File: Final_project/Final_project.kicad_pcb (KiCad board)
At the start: 2 copper layers, 66 x 37 mm, 56 parts, among them J1 USB4105-GF-A, J2 Conn_01x04, J4 LEFT, J5 RIGHT, U1 RP2040, U2 MCP1702T-3302E_CB, U3 W25Q128JV, U4 ESP32-WROOM-32, U5 LM393D, Y1 12MHz

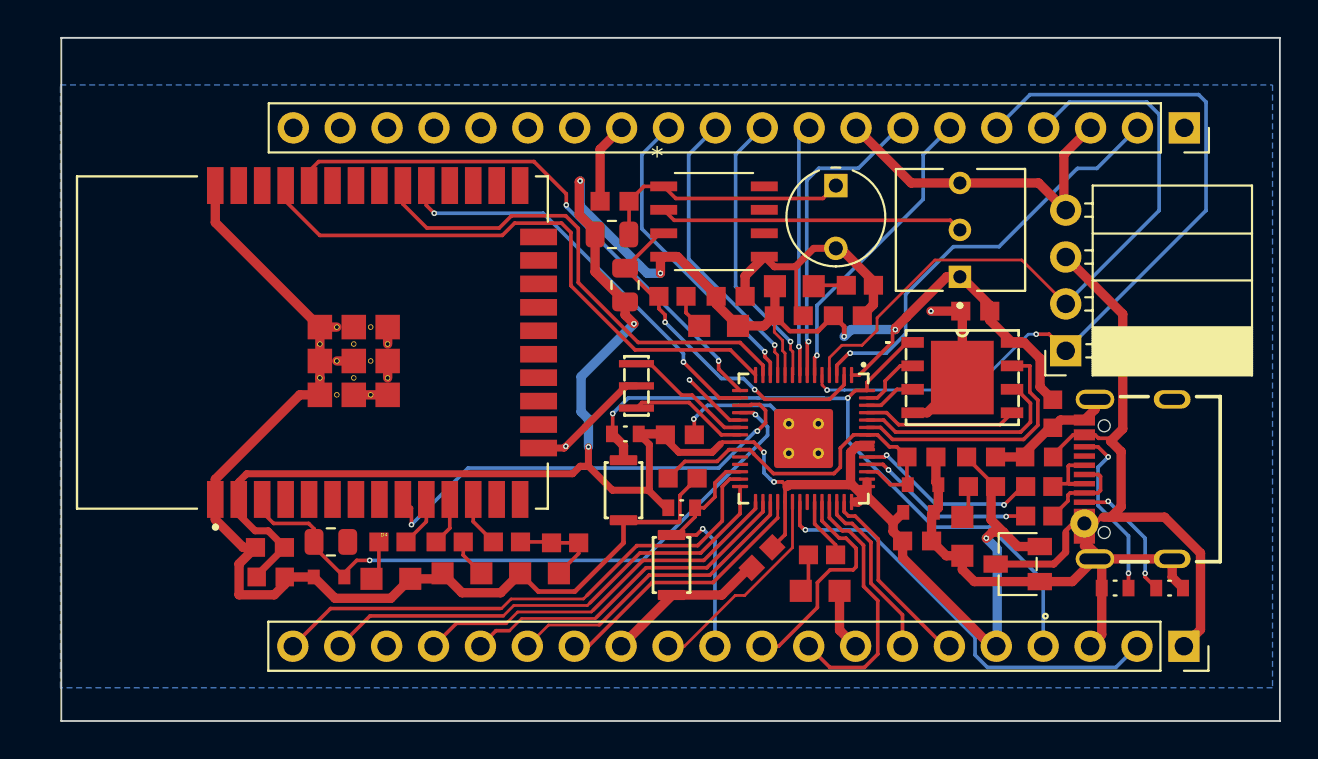
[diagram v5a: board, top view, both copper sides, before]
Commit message: Add 3d, fixing vias and layout issues
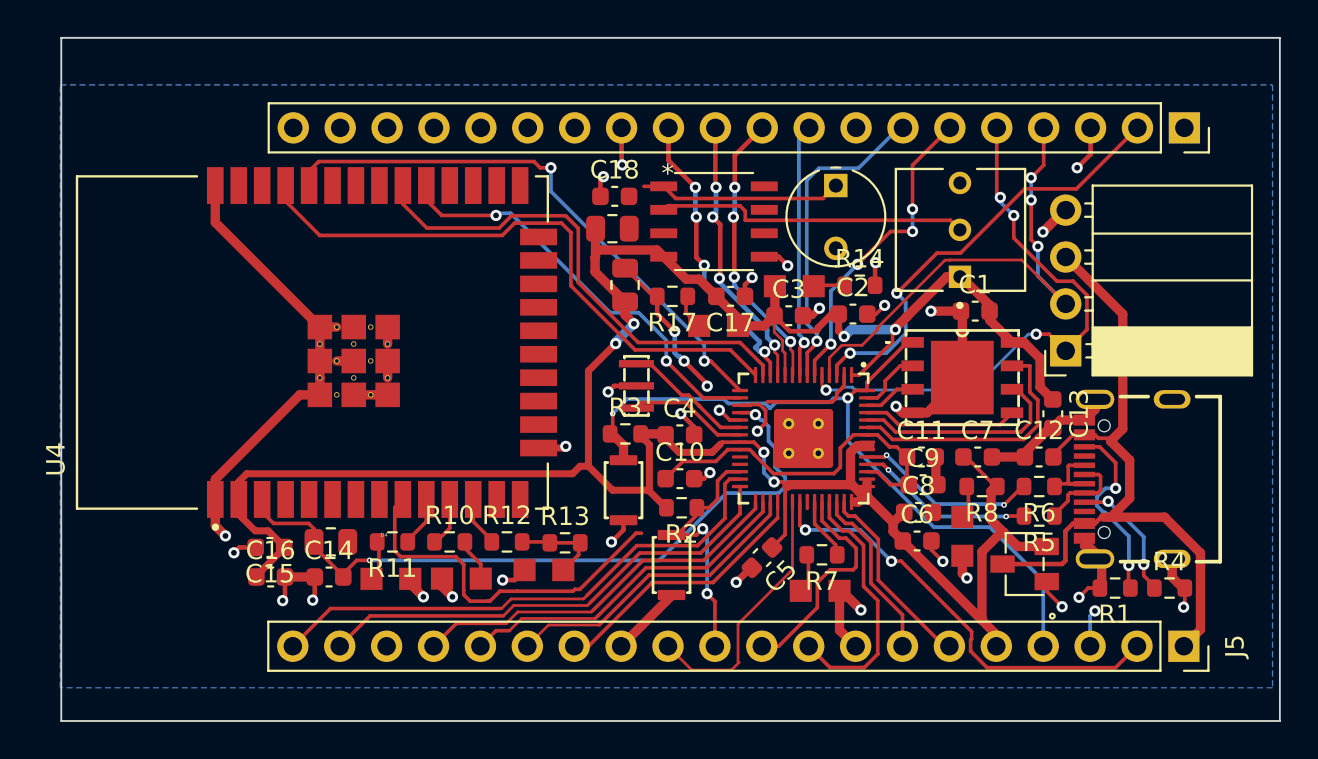
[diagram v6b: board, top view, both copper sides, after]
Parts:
- C1, C10, C11, C15, C17, C18, C2, C3, C4, C5, C6, C7: footprint Final_project:CL10B104JB8NNNC -> Capacitor_SMD:C_0603_1608Metric
- C12, C13, C16: footprint Final_project:GRM188R61E106KA73D -> Capacitor_SMD:C_0603_1608Metric
- C14, C8, C9: footprint Final_project:CL10B105KA8NNNC -> Capacitor_SMD:C_0603_1608Metric
- R1, R2, R3, R4: footprint Final_project:RES_ERJ3EKF5101V -> Resistor_SMD:R_0603_1608Metric
- R10, R11, R12, R13, R14, R17, R5, R6, R7, R8: footprint Final_project:RC0603FR-071KL -> Resistor_SMD:R_0603_1608Metric
- R9: value 10K R -> 10K
- moved U2 0.37 mm to (142.8, 87.2)
- moved R15 0.31 mm to (120.4, 69.0)
- moved D5 0.29 mm to (116.7, 87.5)
- moved C2 0.29 mm to (133.5, 73.7)
- moved D3 0.29 mm to (112.3, 88.0)
- moved C18 0.27 mm to (120.6, 67.3)
- moved C7 0.18 mm to (140.2, 81.4)
- moved C10 0.15 mm to (124.1, 82.6)
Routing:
- net GND: track 177.9 -> 104.2 mm, vias 4 -> 32
- net /GPIO3: track 44.3 -> 30.7 mm, vias 2 -> 4
- net /GPIO2: track 36.8 -> 27.6 mm, vias 0 -> 3
- net +3V3: track 150.0 -> 141.2 mm, vias 9 -> 6
- net /GPIO0: track 19.2 -> 14.0 mm, vias 2 -> 3
- net /GPIO22: track 11.4 -> 14.5 mm
- net /GPIO15: track 35.7 -> 38.7 mm
- net /Light_Sensing/AO: track 13.9 -> 11.0 mm
- net /GPIO14: track 25.2 -> 22.9 mm, vias 2 -> 1
- net /GPIO8: track 16.0 -> 15.0 mm, vias 1 -> 4
- net /GPIO9: track 16.9 -> 16.0 mm, vias 1 -> 4
- net Net-(J1-PadB5): track 9.53 -> 10.3 mm
- net /GPIO1: track 23.5 -> 24.2 mm, vias 1 -> 2
- net /GPIO4: track 16.4 -> 17.1 mm, vias 1 -> 4
- net /GPIO12: track 30.2 -> 30.7 mm
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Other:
- board text added: "Spotify Reader with Light/Dark Sensing Lauren Xiong and Melissa Kazazic Eclectronics FA 2022"

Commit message: fixed several problems
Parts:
- moved R16 1.11 mm to (120.4, 71.2), turned to 180 degrees
- moved C10 0.28 mm to (123.8, 82.5)
- moved R3 0.15 mm to (121.0, 80.2)
- moved R14 0.11 mm to (133.8, 72.0)
- turned R15 to 180 degrees
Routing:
- net /GPIO0: track 14.0 -> 27.4 mm, vias 3 -> 4
- net /GPIO14: track 22.9 -> 32.9 mm, vias 1 -> 2
- net GND: track 104.2 -> 111.1 mm, vias 32 -> 31
- net /Light_Sensing/AO: track 11.0 -> 14.5 mm
- net /GPIO15: track 38.7 -> 35.8 mm
- net +3V3: track 141.2 -> 142.8 mm
- net /GPIO13: track 23.0 -> 23.9 mm
- net /GPIO12: track 30.7 -> 31.4 mm
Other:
- board size 66 x 37 mm -> 66 x 34.6 mm

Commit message: rewired some GND pins
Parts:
- moved C9 0.22 mm to (137.1, 82.9)
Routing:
- net GND: track 111.1 -> 109.9 mm, vias 31 -> 33
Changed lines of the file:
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@@
   )
   (footprint "Capacitor_SMD:C_0603_1608Metric" (layer "F.Cu")
-    (at 137.2722 82.9)
+    (at 137.05 82.9)
     (descr "Capacitor SMD 0603 (1608 Metric), square (rectangular) end terminal, IPC_7351 nominal, (Body size source: IPC-SM-782 page 76, https://www.pcb-3d.com/wordpress/wp-content/uploads/ipc-sm-782a_amendment_1_and_2.pdf), generated with kicad-footprint-generator")
     (tags "capacitor")
@@
   (segment (start 139.4 73.584) (end 139.316 73.5) (width 0.508) (layer "F.Cu") (net 1))
   (segment (start 98.94 66.7) (end 98.94 68.7) (width 0.508) (layer "F.Cu") (net 1))
+  (segment (start 137.026125 85.176675) (end 137.8028 84.4) (width 0.2) (layer "F.Cu") (net 1))
   (segment (start 144.8054 89.5096) (end 143.9686 88.6728) (width 0.2) (layer "F.Cu") (net 1))
-  (segment (start 137.968 82.768) (end 138.1 82.9) (width 0.508) (layer "F.Cu") (net 1))
   (segment (start 137.495 79.005) (end 136.7076 79.005) (width 0.508) (layer "F.Cu") (net 1))
   (segment (start 132.317538 72.85) (end 133.775 72.85) (width 0.2) (layer "F.Cu") (net 1))
@@
   (segment (start 116.45 80.915) (end 117.831 80.915) (width 0.381) (layer "F.Cu") (net 1))
   (segment (start 126.800706 79.4) (end 127.3625 79.4) (width 0.2) (layer "F.Cu") (net 1))
+  (segment (start 137.959 81.4) (end 137.959 81.559) (width 0.2) (layer "F.Cu") (net 1))
   (segment (start 150.765 86.92) (end 150.765 87.915) (width 0.508) (layer "F.Cu") (net 1))
   (segment (start 98.94 68.7) (end 104.605 74.365) (width 0.508) (layer "F.Cu") (net 1))
@@
   (segment (start 135.280132 73.102175) (end 134.722307 73.66) (width 0.2) (layer "F.Cu") (net 1))
   (segment (start 144.949 68.03) (end 145 68.03) (width 0.508) (layer "F.Cu") (net 1))
+  (segment (start 137.959 81.559) (end 138.65 82.25) (width 0.2) (layer "F.Cu") (net 1))
   (segment (start 124.875 79.7741) (end 124.1552 79.0543) (width 0.25) (layer "F.Cu") (net 1))
   (segment (start 146.85 88.5) (end 146.2214 88.5) (width 0.2) (layer "F.Cu") (net 1))
@@
   (segment (start 128.67415 70.555) (end 129.455 70.555) (width 0.25) (layer "F.Cu") (net 1))
   (segment (start 143.9686 88.6728) (end 143.9686 88.148201) (width 0.2) (layer "F.Cu") (net 1))
+  (segment (start 137.825 82.9) (end 138 82.9) (width 0.381) (layer "F.Cu") (net 1))
   (segment (start 146.585 78.825) (end 146.01 79.4) (width 0.508) (layer "F.Cu") (net 1))
   (segment (start 108.275 77.1175) (end 108.275 76.2) (width 0.508) (layer "F.Cu") (net 1))
@@
   (segment (start 111.218 87.9856) (end 111.218 88.4088) (width 0.508) (layer "F.Cu") (net 1))
   (segment (start 124.875 80.2) (end 124.875 79.7741) (width 0.25) (layer "F.Cu") (net 1))
-  (segment (start 137.8028 84.4) (end 137.8028 85.8722) (width 0.381) (layer "F.Cu") (net 1))
   (segment (start 131.417538 73.75) (end 132.317538 72.85) (width 0.2) (layer "F.Cu") (net 1))
   (segment (start 123.65 88.875) (end 123.65 88.92) (width 0.508) (layer "F.Cu") (net 1))
@@
   (segment (start 98.94 85.1224) (end 99.4918 85.6742) (width 0.508) (layer "F.Cu") (net 1))
   (segment (start 127.626 72.7) (end 127.626 72.0688) (width 0.25) (layer "F.Cu") (net 1))
-  (segment (start 137.968 81.4) (end 137.968 82.768) (width 0.508) (layer "F.Cu") (net 1))
   (segment (start 146.95 88.5) (end 146.95 87.285) (width 0.508) (layer "F.Cu") (net 1))
   (segment (start 120.5446 77.55) (end 120.2182 77.8764) (width 0.25) (layer "F.Cu") (net 1))
@@
   (segment (start 137.734 84.5216) (end 137.8556 84.4) (width 0.508) (layer "F.Cu") (net 1))
   (segment (start 106.44 76.2) (end 105.5225 76.2) (width 0.508) (layer "F.Cu") (net 1))
+  (segment (start 136.982273 85.176675) (end 137.026125 85.176675) (width 0.2) (layer "F.Cu") (net 1))
   (segment (start 136.159611 79.005) (end 135.810034 78.655423) (width 0.508) (layer "F.Cu") (net 1))
   (segment (start 133.775 72.85) (end 134.625 72) (width 0.2) (layer "F.Cu") (net 1))
@@
   (segment (start 121.75 77.55) (end 120.5446 77.55) (width 0.25) (layer "F.Cu") (net 1))
   (segment (start 121.05 84.825) (end 121.05 85.3504) (width 0.254) (layer "F.Cu") (net 1))
-  (segment (start 138.0472 82.9) (end 138.0472 84.1556) (width 0.381) (layer "F.Cu") (net 1))
   (segment (start 146.01 79.4) (end 144.718 79.4) (width 0.508) (layer "F.Cu") (net 1))
   (segment (start 132.75 88.65) (end 132.8714 88.65) (width 0.508) (layer "F.Cu") (net 1))
@@
   (segment (start 137.8028 85.8722) (end 137.725 85.95) (width 0.381) (layer "F.Cu") (net 1))
   (segment (start 144.9 67.93) (end 145 68.03) (width 0.508) (layer "F.Cu") (net 1))
+  (segment (start 138 82.9) (end 138.65 82.25) (width 0.1524) (layer "F.Cu") (net 1))
   (segment (start 134.585 71.886976) (end 134.585 72.1) (width 0.508) (layer "F.Cu") (net 1))
+  (segment (start 136.982273 85.207273) (end 136.982273 85.176675) (width 0.2) (layer "F.Cu") (net 1))
   (segment (start 98.94 83.7) (end 98.94 85.1224) (width 0.508) (layer "F.Cu") (net 1))
   (segment (start 132.75 88.65) (end 132.75 90.78) (width 0.508) (layer "F.Cu") (net 1))
+  (segment (start 137.825 84.3778) (end 137.8028 84.4) (width 0.381) (layer "F.Cu") (net 1))
   (segment (start 125.714852 82.264852) (end 125.529704 82.45) (width 0.25) (layer "F.Cu") (net 1))
-  (segment (start 138.0472 84.1556) (end 137.8028 84.4) (width 0.381) (layer "F.Cu") (net 1))
   (segment (start 143.764 69.215) (end 144.949 68.03) (width 0.508) (layer "F.Cu") (net 1))
   (segment (start 119.7988 67.2846) (end 119.7988 66.3832) (width 0.25) (layer "F.Cu") (net 1))
   (segment (start 134.625 72) (end 134.625 70.951901) (width 0.25) (layer "F.Cu") (net 1))
   (segment (start 105.5225 74.365) (end 104.605 74.365) (width 0.508) (layer "F.Cu") (net 1))
+  (via (at 138.65 82.25) (size 0.6096) (drill 0.3048) (layers "F.Cu" "B.Cu") (net 1))
   (via (at 144.8054 89.5096) (size 0.6096) (drill 0.3048) (layers "F.Cu" "B.Cu") (net 1))
   (via (at 99.4918 85.6742) (size 0.6096) (drill 0.3048) (layers "F.Cu" "B.Cu") (net 1))
@@
   (via (at 110.2106 88.9762) (size 0.6096) (drill 0.3048) (layers "F.Cu" "B.Cu") (net 1))
   (via (at 114.5032 88.0671) (size 0.6096) (drill 0.3048) (layers "F.Cu" "B.Cu") (net 1))
+  (via (at 136.982273 85.176675) (size 0.6096) (drill 0.3048) (layers "F.Cu" "B.Cu") (net 1))
   (via (at 119.9642 66.2178) (size 0.6096) (drill 0.3048) (layers "F.Cu" "B.Cu") (net 1))
   (via (at 127.1524 88.1888) (size 0.6096) (drill 0.3048) (layers "F.Cu" "B.Cu") (net 1))
